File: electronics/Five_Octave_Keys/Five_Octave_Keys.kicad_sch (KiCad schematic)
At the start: 123 parts, among them J1 FFC Connector, SW1 Key Esc, SW10 Key 9, SW11 Key 0, SW12 Key -, SW13 Key =, SW14 Key \, SW15 Key `, SW16 Key Tab, SW17 Key Q, SW18 Key W, SW19 Key E, SW2 Key 1, SW20 Key R, SW21 Key T, SW22 Key Y, SW23 Key U, SW24 Key I, SW25 Key O, SW26 Key P, SW27 Key [, SW28 Key ], SW29 Key BS, SW3 Key 2, SW30 Key Caps, SW31 Key A, SW32 Key S, SW33 Key D, SW34 Key F, SW35 Key G, SW36 Key H, SW37 Key J, SW38 Key K, SW39 Key L, SW4 Key 3, SW40 Key ;, SW41 Key ', SW42 Key Return, SW43 Key Shift, SW44 Key Z, SW45 Key X, SW46 Key C, SW47 Key V, SW48 Key B, SW49 Key N, SW5 Key 4, SW50 Key M, SW51 Key ,, SW52 Key ., SW53 Key /, SW54 Key Shift, SW55 Key Fn, SW56 Key Ctrl, SW57 Key Opt, SW58 Key Cmd, SW59 Key Space, SW6 Key 5, SW60 Key Cmd, SW61 Key MO(1), SW7 Key 6, SW8 Key 7, SW9 Key 8

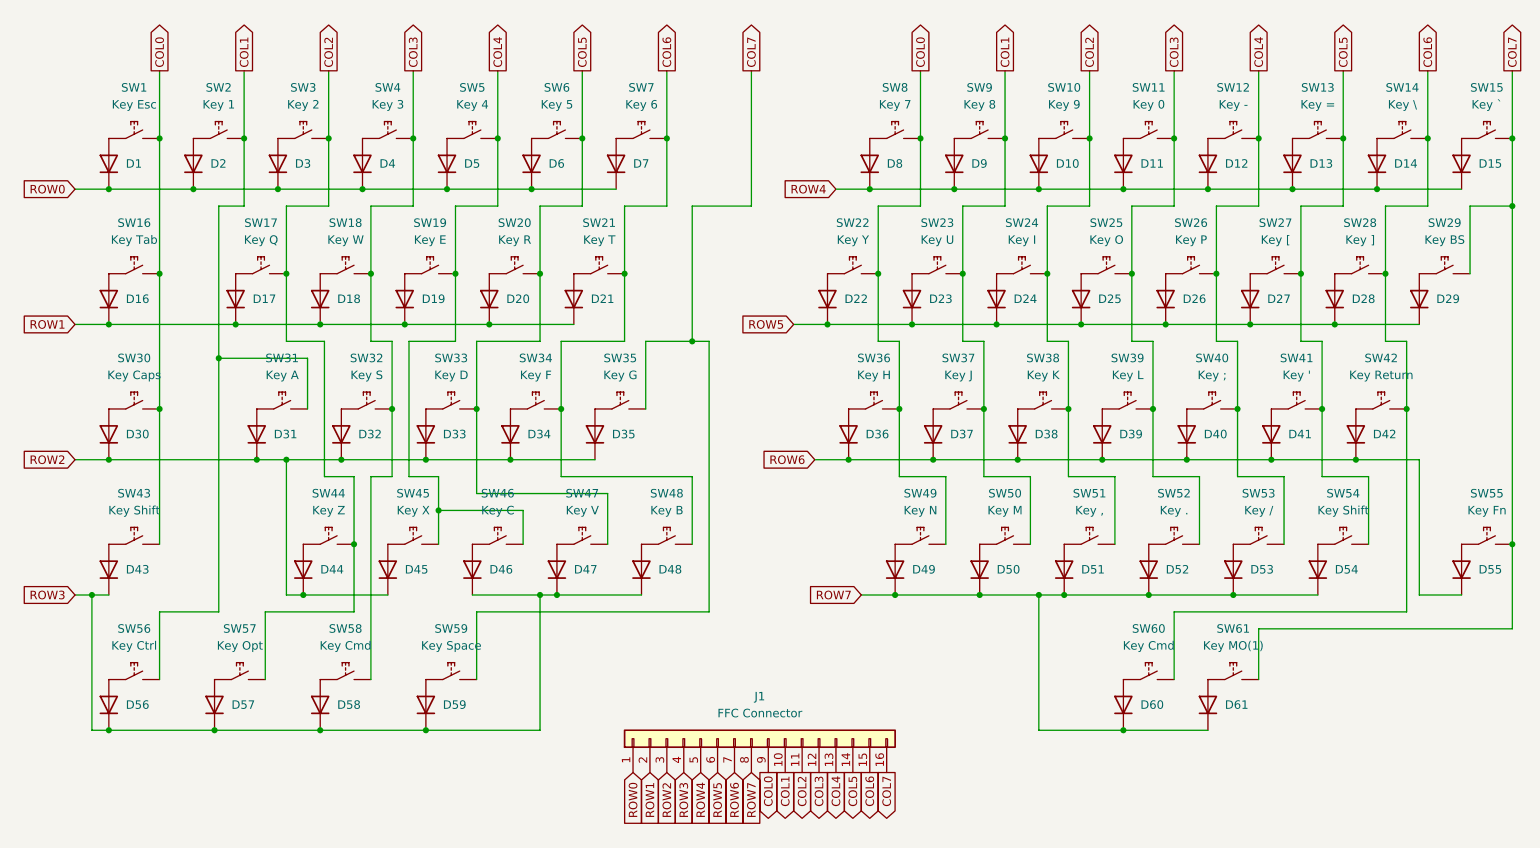
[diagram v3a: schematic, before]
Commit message: Adjust key-matrix
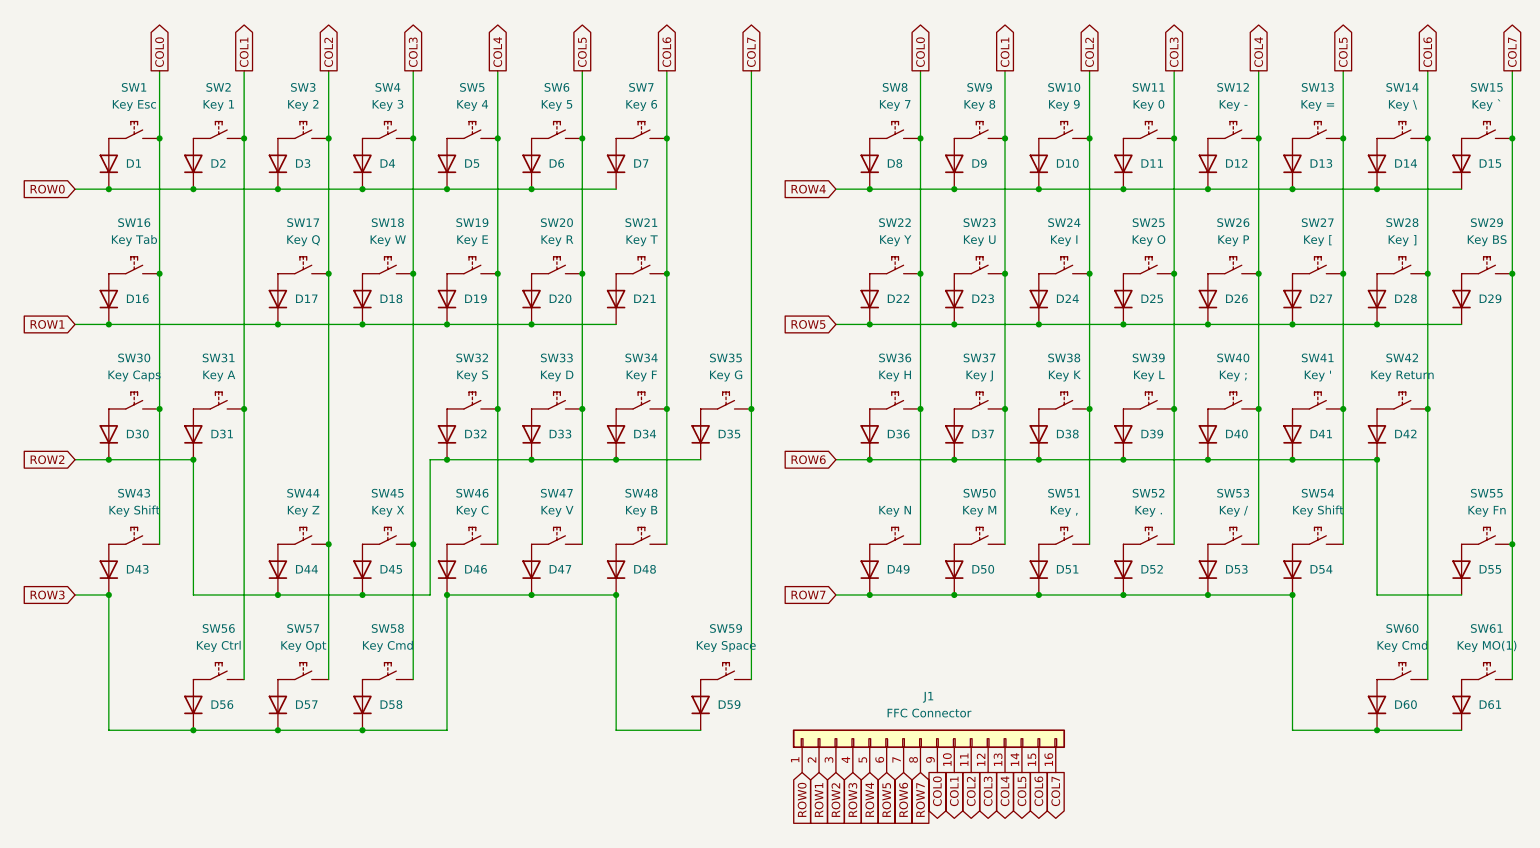
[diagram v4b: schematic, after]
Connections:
- net COL3: now also SW45.2; no longer SW32.2
- net COL4: now also SW32.2; no longer SW45.2
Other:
- moved on the sheet: D17, D18, D19, D20, D21, D22, D23, D24, D25, D26, D27, D28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

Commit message: Adjust key-matrix
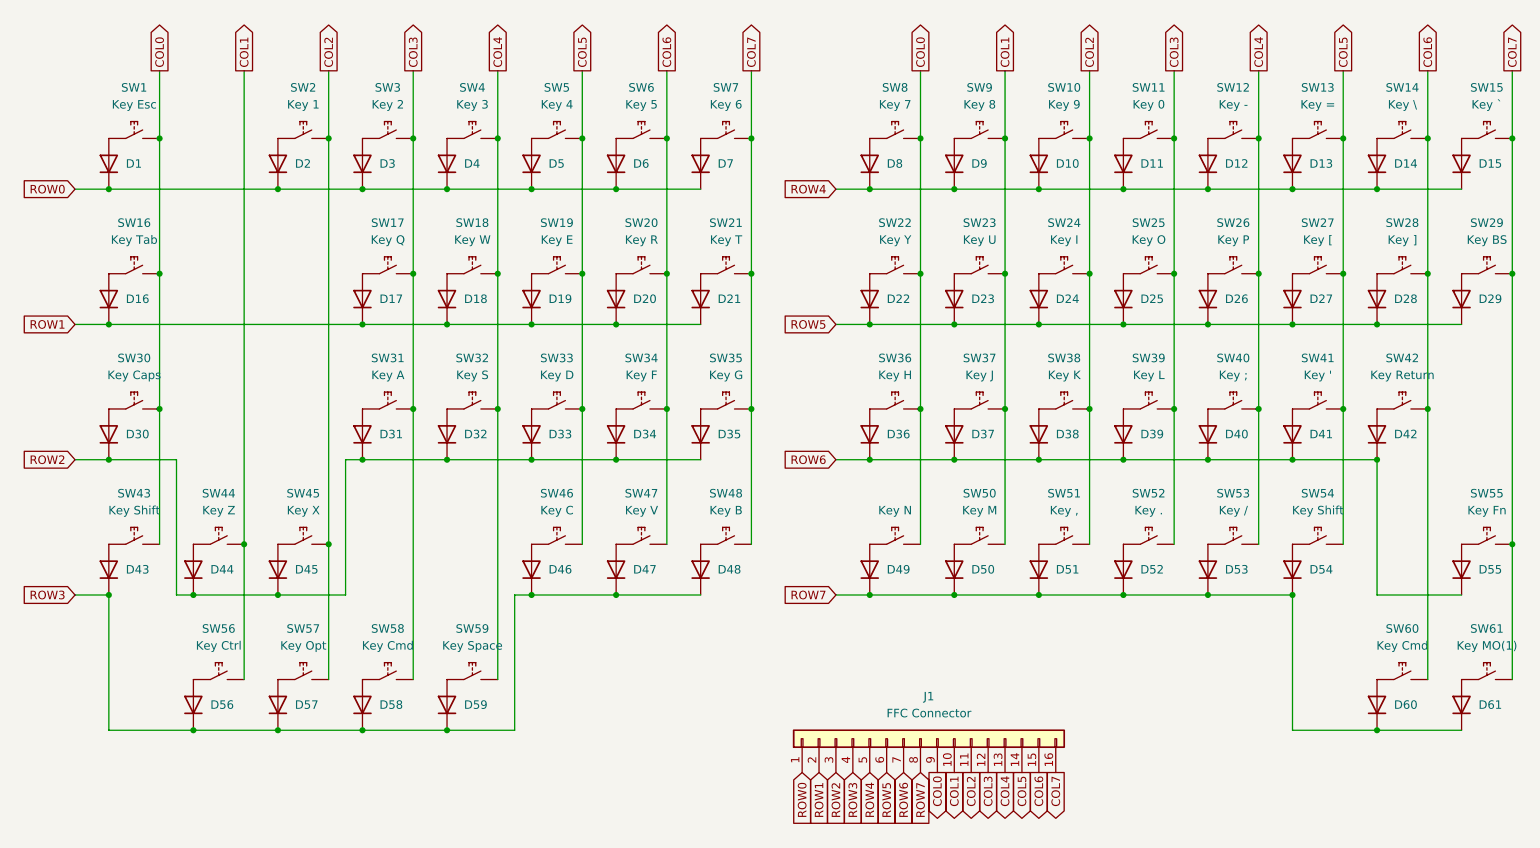
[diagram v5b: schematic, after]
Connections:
- net COL1: now also SW44.2; no longer SW2.2, SW31.2
- net COL2: now also SW2.2, SW45.2; no longer SW17.2, SW3.2, SW44.2
- net COL3: now also SW17.2, SW3.2, SW31.2; no longer SW18.2, SW4.2, SW45.2
- net COL4: now also SW18.2, SW4.2, SW59.2; no longer SW19.2, SW46.2, SW5.2
- net COL5: now also SW19.2, SW46.2, SW5.2; no longer SW20.2, SW47.2, SW6.2
- net COL6: now also SW20.2, SW47.2, SW6.2; no longer SW21.2, SW48.2, SW7.2
- net COL7: now also SW21.2, SW48.2, SW7.2; no longer SW59.2
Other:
- moved on the sheet: D17, D18, D19, D2, D20, D21, D3, D31, D4, D44, D45, D46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

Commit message: Update
- Assign JLCPCB part number to SW1-61
- GH60 compatible
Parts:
- SW1, SW10, SW11, SW12, SW13, SW14, SW15, SW16, SW17, SW18, SW19, SW2, SW20, SW21, SW22, SW23, SW24, SW25, SW26, SW27, SW28, SW29, SW3, SW30, SW31, SW32, SW33, SW34, SW35, SW36, SW37, SW38, SW39, SW4, SW40, SW41, SW42, SW43, SW44, SW45, SW46, SW47, SW48, SW49, SW5, SW50, SW51, SW52, SW53, SW54, SW55, SW56, SW57, SW58, SW59, SW6, SW60, SW61, SW7, SW8, SW9: LCSC (none) -> C5156480
